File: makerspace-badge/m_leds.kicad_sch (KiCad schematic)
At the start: 66 parts

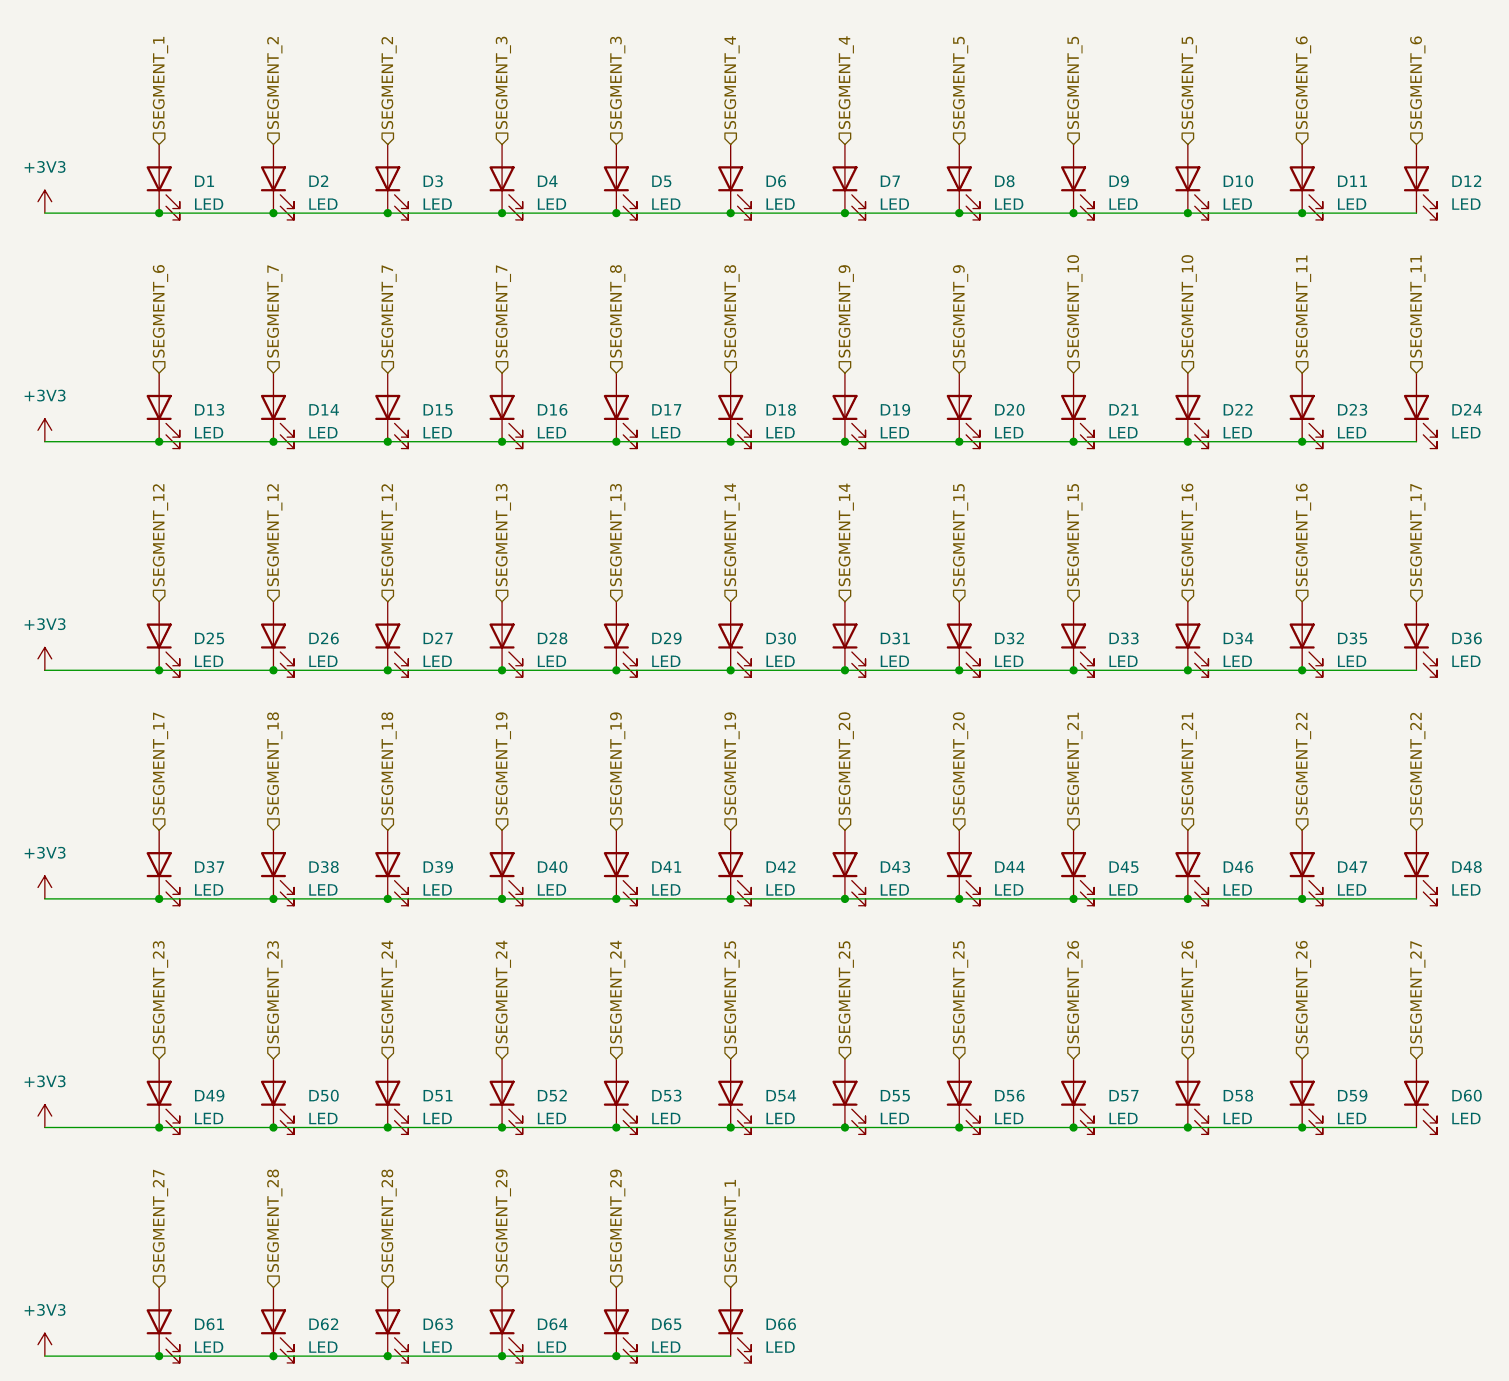
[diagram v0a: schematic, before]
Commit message: Maker Space badge, revision B
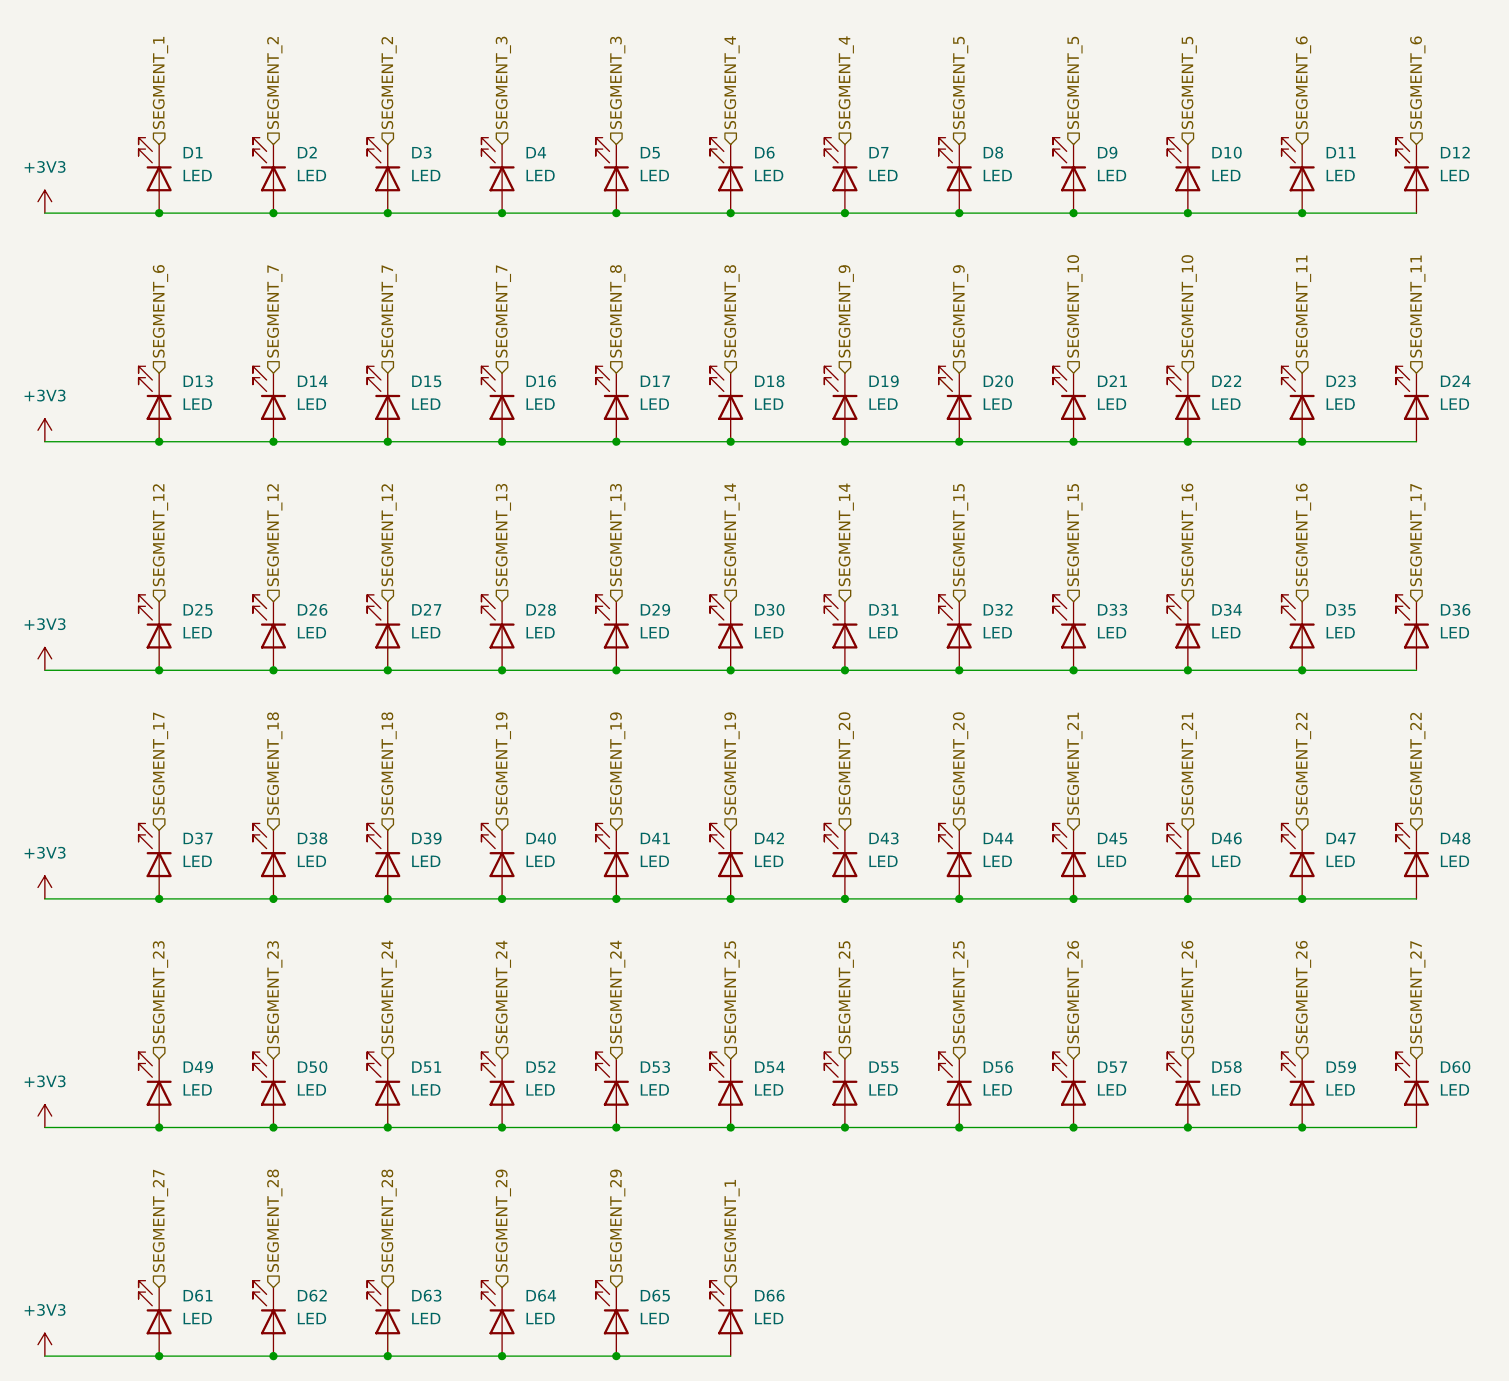
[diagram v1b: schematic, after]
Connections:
- net +3V3: now also D1.2 (A), D10.2 (A), D11.2 (A), D12.2 (A), D13.2 (A), D14.2 (A), D15.2 (A), D16.2 (A), D17.2 (A), D18.2 (A), D19.2 (A), D2.2 (A), D20.2 (A), D21.2 (A), D22.2 (A), D23.2 (A), D24.2 (A), D25.2 (A), D26.2 (A), D27.2 (A), D28.2 (A), D29.2 (A), D3.2 (A), D30.2 (A), D31.2 (A), D32.2 (A), D33.2 (A), D34.2 (A), D35.2 (A), D36.2 (A), D37.2 (A), D38.2 (A), D39.2 (A), D4.2 (A), D40.2 (A), D41.2 (A), D42.2 (A), D43.2 (A), D44.2 (A), D45.2 (A), D46.2 (A), D47.2 (A), D48.2 (A), D49.2 (A), D5.2 (A), D50.2 (A), D51.2 (A), D52.2 (A), D53.2 (A), D54.2 (A), D55.2 (A), D56.2 (A), D57.2 (A), D58.2 (A), D59.2 (A), D6.2 (A), D60.2 (A), D61.2 (A), D62.2 (A), D63.2 (A), D64.2 (A), D65.2 (A), D66.2 (A), D7.2 (A), D8.2 (A), D9.2 (A); no longer D1.1 (K), D10.1 (K), D11.1 (K), D12.1 (K), D13.1 (K), D14.1 (K), D15.1 (K), D16.1 (K), D17.1 (K), D18.1 (K), D19.1 (K), D2.1 (K), D20.1 (K), D21.1 (K), D22.1 (K), D23.1 (K), D24.1 (K), D25.1 (K), D26.1 (K), D27.1 (K), D28.1 (K), D29.1 (K), D3.1 (K), D30.1 (K), D31.1 (K), D32.1 (K), D33.1 (K), D34.1 (K), D35.1 (K), D36.1 (K), D37.1 (K), D38.1 (K), D39.1 (K), D4.1 (K), D40.1 (K), D41.1 (K), D42.1 (K), D43.1 (K), D44.1 (K), D45.1 (K), D46.1 (K), D47.1 (K), D48.1 (K), D49.1 (K), D5.1 (K), D50.1 (K), D51.1 (K), D52.1 (K), D53.1 (K), D54.1 (K), D55.1 (K), D56.1 (K), D57.1 (K), D58.1 (K), D59.1 (K), D6.1 (K), D60.1 (K), D61.1 (K), D62.1 (K), D63.1 (K), D64.1 (K), D65.1 (K), D66.1 (K), D7.1 (K), D8.1 (K), D9.1 (K)
- net SEGMENT_1: now also D1.1 (K), D66.1 (K); no longer D1.2 (A), D66.2 (A)
- net SEGMENT_10: now also D21.1 (K), D22.1 (K); no longer D21.2 (A), D22.2 (A)
- net SEGMENT_11: now also D23.1 (K), D24.1 (K); no longer D23.2 (A), D24.2 (A)
- net SEGMENT_12: now also D25.1 (K), D26.1 (K), D27.1 (K); no longer D25.2 (A), D26.2 (A), D27.2 (A)
- net SEGMENT_13: now also D28.1 (K), D29.1 (K); no longer D28.2 (A), D29.2 (A)
- net SEGMENT_14: now also D30.1 (K), D31.1 (K); no longer D30.2 (A), D31.2 (A)
- net SEGMENT_15: now also D32.1 (K), D33.1 (K); no longer D32.2 (A), D33.2 (A)
- net SEGMENT_16: now also D34.1 (K), D35.1 (K); no longer D34.2 (A), D35.2 (A)
- net SEGMENT_17: now also D36.1 (K), D37.1 (K); no longer D36.2 (A), D37.2 (A)
- net SEGMENT_18: now also D38.1 (K), D39.1 (K); no longer D38.2 (A), D39.2 (A)
- net SEGMENT_19: now also D40.1 (K), D41.1 (K), D42.1 (K); no longer D40.2 (A), D41.2 (A), D42.2 (A)
- net SEGMENT_2: now also D2.1 (K), D3.1 (K); no longer D2.2 (A), D3.2 (A)
- net SEGMENT_20: now also D43.1 (K), D44.1 (K); no longer D43.2 (A), D44.2 (A)
- net SEGMENT_21: now also D45.1 (K), D46.1 (K); no longer D45.2 (A), D46.2 (A)
- net SEGMENT_22: now also D47.1 (K), D48.1 (K); no longer D47.2 (A), D48.2 (A)
- net SEGMENT_23: now also D49.1 (K), D50.1 (K); no longer D49.2 (A), D50.2 (A)
- net SEGMENT_24: now also D51.1 (K), D52.1 (K), D53.1 (K); no longer D51.2 (A), D52.2 (A), D53.2 (A)
- net SEGMENT_25: now also D54.1 (K), D55.1 (K), D56.1 (K); no longer D54.2 (A), D55.2 (A), D56.2 (A)
- net SEGMENT_26: now also D57.1 (K), D58.1 (K), D59.1 (K); no longer D57.2 (A), D58.2 (A), D59.2 (A)
- net SEGMENT_27: now also D60.1 (K), D61.1 (K); no longer D60.2 (A), D61.2 (A)
- net SEGMENT_28: now also D62.1 (K), D63.1 (K); no longer D62.2 (A), D63.2 (A)
- net SEGMENT_29: now also D64.1 (K), D65.1 (K); no longer D64.2 (A), D65.2 (A)
- net SEGMENT_3: now also D4.1 (K), D5.1 (K); no longer D4.2 (A), D5.2 (A)
- net SEGMENT_4: now also D6.1 (K), D7.1 (K); no longer D6.2 (A), D7.2 (A)
- net SEGMENT_5: now also D10.1 (K), D8.1 (K), D9.1 (K); no longer D10.2 (A), D8.2 (A), D9.2 (A)
- net SEGMENT_6: now also D11.1 (K), D12.1 (K), D13.1 (K); no longer D11.2 (A), D12.2 (A), D13.2 (A)
- net SEGMENT_7: now also D14.1 (K), D15.1 (K), D16.1 (K); no longer D14.2 (A), D15.2 (A), D16.2 (A)
- net SEGMENT_8: now also D17.1 (K), D18.1 (K); no longer D17.2 (A), D18.2 (A)
- net SEGMENT_9: now also D19.1 (K), D20.1 (K); no longer D19.2 (A), D20.2 (A)
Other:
- moved on the sheet: D1, D10, D11, D12, D13, D14, D15, D16, D17, D18, D19, D2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
